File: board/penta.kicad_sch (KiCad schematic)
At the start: 184 parts, among them J1 USB_C_Receptacle, J2 USB_C_Receptacle, J3 Conn_01x03_Pin, Q1 Q_NMOS_SGD, SW1 SW_Push, U1 3.3V LDO, U2 RP2040, U3 QSPI Flash, U4 MSUSB30, U5 USBLC6-2P6, Y1 12MHz

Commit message: kicad format update
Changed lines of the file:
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@@
 (kicad_sch
-	(version 20231120)
+	(version 20250114)
 	(generator "eeschema")
-	(generator_version "8.0")
+	(generator_version "9.0")
 	(paper "A4")
+	(text "layout close to rp2040"
+		(exclude_from_sim no)
+		(at 121.92 44.45 0)
+		(effects
+			(font
+				(size 1.27 1.27)
+			)
+			(justify left bottom)
+		)
+	)
+	(text "LRCLK gpio must be CLK+1"
+		(exclude_from_sim no)
+		(at 214.122 94.742 0)
+		(effects
+			(font
+				(size 1.27 1.27)
+			)
+			(justify left)
+		)
+	)
+	(text "Pixels Load Switch"
+		(exclude_from_sim no)
+		(at 261.366 78.486 0)
+		(effects
+			(font
+				(size 1.5 1.5)
+			)
+		)
+	)
+	(text "pio requirement:\ntouch pins must be contiguous gpios"
+		(exclude_from_sim no)
+		(at 231.394 50.038 0)
+		(effects
+			(font
+				(size 1.27 1.27)
+			)
+			(justify left)
+		)
+	)
 	(junction
 		(at 397.51 234.95)
@@
 		)
 	)
-	(text "layout close to rp2040"
-		(exclude_from_sim no)
-		(at 121.92 44.45 0)
-		(effects
-			(font
-				(size 1.27 1.27)
-			)
-			(justify left bottom)
-		)
-	)
-	(text "LRCLK gpio must be CLK+1"
-		(exclude_from_sim no)
-		(at 214.122 94.742 0)
-		(effects
-			(font
-				(size 1.27 1.27)
-			)
-			(justify left)
-		)
-	)
-	(text "Pixels Load Switch"
-		(exclude_from_sim no)
-		(at 261.366 78.486 0)
-		(effects
-			(font
-				(size 1.5 1.5)
-			)
-		)
-	)
-	(text "pio requirement:\ntouch pins must be contiguous gpios"
-		(exclude_from_sim no)
-		(at 231.394 50.038 0)
-		(effects
-			(font
-				(size 1.27 1.27)
-			)
-			(justify left)
-		)
-	)
 	(label "UART0_TX"
 		(at 201.93 85.09 0)
-		(fields_autoplaced yes)
 		(effects
 			(font
@@
 	(label "LED_DATA"
 		(at 328.93 26.67 180)
-		(fields_autoplaced yes)
 		(effects
 			(font
@@
 	(label "EN_PIXELS"
 		(at 201.93 100.33 0)
-		(fields_autoplaced yes)
 		(effects
 			(font
@@
 	(label "PDM_LRCLK"
 		(at 261.62 138.43 0)
-		(fields_autoplaced yes)
 		(effects
 			(font
@@
 	(label "USB_D+"
 		(at 69.85 96.52 180)
-		(fields_autoplaced yes)
 		(effects
 			(font
@@
 	(label "~{USB_BOOT}"
 		(at 123.19 62.23 0)
-		(fields_autoplaced yes)
 		(effects
 			(font
@@
 	(label "SWCLK"
 		(at 143.51 110.49 0)
-		(fields_autoplaced yes)
 		(effects
 			(font
@@
 	(label "USB_D-_PORT"
 		(at 57.15 59.69 270)
-		(fields_autoplaced yes)
 		(effects
 			(font
@@
 	(label "USB_D-_IN"
 		(at 44.45 38.1 0)
-		(fields_autoplaced yes)
 		(effects
 			(font
@@
 	(label "USB_D+"
 		(at 125.73 48.26 0)
-		(fields_autoplaced yes)
 		(effects
 			(font
@@
 	(label "PXL_GND"
 		(at 264.16 87.63 0)
-		(fields_autoplaced yes)
 		(effects
 			(font
@@
 	(label "USB2_D+"
 		(at 45.72 140.97 0)
-		(fields_autoplaced yes)
 		(effects
 			(font
@@
 	(label "QSPI_SCK"
 		(at 167.64 157.48 0)
-		(fields_autoplaced yes)
 		(effects
 			(font
@@
 	(label "QSPI3"
 		(at 142.24 74.93 0)
-		(fields_autoplaced yes)
 		(effects
 			(font
@@
 	(label "USB2_D-"
 		(at 45.72 138.43 0)
-		(fields_autoplaced yes)
 		(effects
 			(font
@@
 	(label "PXL_GND"
 		(at 331.47 274.32 180)
-		(fields_autoplaced yes)
 		(effects
 			(font
@@
 	(label "PXL_GND"
 		(at 331.47 34.29 180)
-		(fields_autoplaced yes)
 		(effects
 			(font
@@
 	(label "UART0_RX"
 		(at 201.93 87.63 0)
-		(fields_autoplaced yes)
 		(effects
 			(font
@@
 	(label "PDM_DATA"
 		(at 261.62 140.97 0)
-		(fields_autoplaced yes)
 		(effects
 			(font
@@
 	(label "USB_D+_IN"
 		(at 44.45 40.64 0)
-		(fields_autoplaced yes)
 		(effects
 			(font
@@
 	(label "QSPI1"
 		(at 129.54 153.67 180)
-		(fields_autoplaced yes)
 		(effects
 			(font
@@
 	(label "USB2_D-"
 		(at 222.25 85.09 0)
-		(fields_autoplaced yes)
 		(effects
 			(font
@@
 	(label "EN_PIXELS"
 		(at 252.73 100.33 90)
-		(fields_autoplaced yes)
 		(effects
 			(font
@@
 	(label "QSPI0"
 		(at 142.24 67.31 0)
-		(fields_autoplaced yes)
 		(effects
 			(font
@@
 	(label "USB_D-"
 		(at 92.71 99.06 0)
-		(fields_autoplaced yes)
 		(effects
 			(font
@@
 	(label "USB_D+_PORT"
 		(at 69.85 101.6 180)
-		(fields_autoplaced yes)
 		(effects
 			(font
@@
 	(label "PXL_GND"
 		(at 331.47 114.3 180)
-		(fields_autoplaced yes)
 		(effects
 			(font
@@
 	(label "PXL_GND"
 		(at 331.47 154.94 180)
-		(fields_autoplaced yes)
 		(effects
 			(font
@@
 	(label "UART1_RX"
 		(at 92.71 101.6 0)
-		(fields_autoplaced yes)
 		(effects
 			(font
@@
 	(label "QSPI_SS"
 		(at 142.24 62.23 0)
-		(fields_autoplaced yes)
 		(effects
 			(font
@@
 	(label "PXL_GND"
 		(at 331.47 74.93 180)
-		(fields_autoplaced yes)
 		(effects
 			(font
@@
 	(label "LED_DATA"
 		(at 201.93 59.69 0)
-		(fields_autoplaced yes)
 		(effects
 			(font
@@
 	(label "USB_D+_PORT"
 		(at 54.61 59.69 270)
-		(fields_autoplaced yes)
 		(effects
 			(font
@@
 	(label "PXL_GND"
 		(at 331.47 194.31 180)
-		(fields_autoplaced yes)
 		(effects
 			(font
@@
 	(label "PDM_CLK"
 		(at 261.62 143.51 0)
-		(fields_autoplaced yes)
 		(effects
 			(font
@@
 	(label "USB_D-"
 		(at 125.73 54.61 0)
-		(fields_autoplaced yes)
 		(effects
 			(font
@@
 	(label "PDM_DATA"
 		(at 201.93 95.25 0)
-		(fields_autoplaced yes)
 		(effects
 			(font
@@
 	(label "USB2_D+"
 		(at 222.25 87.63 0)
-		(fields_autoplaced yes)
 		(effects
 			(font
@@
 	(label "USBMUX_SELECT"
 		(at 201.93 102.87 0)
-		(fields_autoplaced yes)
 		(effects
 			(font
@@
 	(label "UART1_RX"
 		(at 201.93 107.95 0)
-		(fields_autoplaced yes)
 		(effects
 			(font
@@
 	(label "PXL_GND"
 		(at 331.47 234.95 180)
-		(fields_autoplaced yes)
 		(effects
 			(font
@@
 	(label "QSPI0"
 		(at 167.64 160.02 0)
-		(fields_autoplaced yes)
 		(effects
 			(font
@@
 	(label "QSPI3"
 		(at 167.64 154.94 0)
-		(fields_autoplaced yes)
 		(effects
 			(font
@@
 	(label "QSPI1"
 		(at 142.24 69.85 0)
-		(fields_autoplaced yes)
 		(effects
 			(font
@@
 	(label "UART1_TX"
 		(at 201.93 105.41 0)
-		(fields_autoplaced yes)
 		(effects
 			(font
@@
 	(label "QSPI_SS"
 		(at 129.54 151.13 180)
-		(fields_autoplaced yes)
 		(effects
 			(font
@@
 	(label "USBMUX_SELECT"
 		(at 69.85 93.98 180)
-		(fields_autoplaced yes)
 		(effects
 			(font
@@
 	(label "PDM_CLK"
 		(at 201.93 90.17 0)
-		(fields_autoplaced yes)
 		(effects
 			(font
@@
 	(label "PDM_LRCLK"
 		(at 201.93 92.71 0)
-		(fields_autoplaced yes)
 		(effects
 			(font
@@
 	(label "QSPI2"
 		(at 142.24 72.39 0)
-		(fields_autoplaced yes)
 		(effects
 			(font
@@
 	(label "SWD"
 		(at 143.51 113.03 0)
-		(fields_autoplaced yes)
 		(effects
 			(font
@@
 	(label "QSPI_SCK"
 		(at 139.7 77.47 0)
-		(fields_autoplaced yes)
 		(effects
 			(font
@@
 	(label "UART1_TX"
 		(at 69.85 99.06 180)
-		(fields_autoplaced yes)
 		(effects
 			(font
@@
 	(label "QSPI2"
 		(at 129.54 156.21 180)
-		(fields_autoplaced yes)
 		(effects
 			(font
@@
 	(label "USB_D-_PORT"
 		(at 92.71 104.14 0)
-		(fields_autoplaced yes)
 		(effects
 			(font
@@
 		)
 	)
+	(embedded_fonts no)
 )

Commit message: mosfet GSD was actually correct so change it back. the dim pixel issue was current leaking through data line, already fixed in software in main
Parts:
- removed Q1: Q_NMOS_SGD, Package_TO_SOT_SMD:SOT-23, symbol Device:Q_NMOS_SGD
- added Q1: Q_NMOS_GSD, symbol Transistor_FET:Q_NMOS_GSD
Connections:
- net EN_PIXELS: now also Q1.1 (G)
- net GND: now also Q1.2 (S)
- net PXL_GND: now also Q1.3 (D)
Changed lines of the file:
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@@
 	)
 	(junction
-		(at 473.71 219.71)
-		(diameter 0)
-		(color 0 0 0 0)
-	)
-	(junction
 		(at 443.23 170.18)
 		(diameter 0)
@@
 	)
 	(junction
-		(at 473.71 59.69)
-		(diameter 0)
-		(color 0 0 0 0)
-	)
-	(junction
 		(at 458.47 74.93)
 		(diameter 0)
@@
 	)
 	(junction
-		(at 473.71 139.7)
-		(diameter 0)
-		(color 0 0 0 0)
-	)
-	(junction
 		(at 336.55 99.06)
 		(diameter 0)
@@
 	(wire
 		(pts
-			(xy 473.71 58.42) (xy 473.71 59.69)
-		)
-		(stroke
-			(width 0)
-			(type default)
-		)
-	)
-	(wire
-		(pts
 			(xy 336.55 139.7) (xy 351.79 139.7)
 		)
@@
 	(wire
 		(pts
-			(xy 473.71 138.43) (xy 473.71 139.7)
-		)
-		(stroke
-			(width 0)
-			(type default)
-		)
-	)
-	(wire
-		(pts
 			(xy 209.55 22.86) (xy 219.71 22.86)
 		)
@@
 	(wire
 		(pts
-			(xy 473.71 218.44) (xy 473.71 219.71)
-		)
-		(stroke
-			(width 0)
-			(type default)
-		)
-	)
-	(wire
-		(pts
 			(xy 50.8 30.48) (xy 50.8 27.94)
 		)
@@
 	)
 	(symbol
-		(lib_id "Device:Q_NMOS_SGD")
-		(at 261.62 100.33 0)
+		(lib_id "power:GND")
+		(at 264.16 107.95 0)
 		(unit 1)
 		(exclude_from_sim no)
@@
 		(on_board yes)
 		(dnp no)
-		(fields_autoplaced yes)
-		(property "Reference" "Q1"
-			(at 266.827 99.1178 0)
-			(effects
-				(font
-					(size 1.27 1.27)
-				)
-				(justify left)
-			)
-		)
-		(property "Value" "Q_NMOS_SGD"
-			(at 266.827 101.5421 0)
-			(effects
-				(font
-					(size 1.27 1.27)
-				)
-				(justify left)
-			)
-		)
-		(property "Footprint" "Package_TO_SOT_SMD:SOT-23"
-			(at 266.7 97.79 0)
+		(property "Reference" "#PWR03"
+			(at 264.16 114.3 0)
 			(effects
 				(font
@@
 			)
 		)
-		(property "Datasheet" "~"
-			(at 261.62 100.33 0)
+		(property "Value" "GND"
+			(at 264.16 112.522 90)
 			(effects
 				(font
 					(size 1.27 1.27)
 				)
-				(hide yes)
 			)
 		)
-		(property "Description" "N-MOSFET transistor, source/gate/drain"
-			(at 261.62 100.33 0)
+		(property "Footprint" ""
+			(at 264.16 107.95 0)
 			(effects
 				(font
@@
 			)
 		)
-		(property "Designation" "SI2302"
-			(at 261.62 100.33 0)
+		(property "Datasheet" ""
+			(at 264.16 107.95 0)
 			(effects
 				(font
@@
 			)
 		)
-		(property "LCSC" "C727152"
-			(at 261.62 100.33 0)
+		(property "Description" "Power symbol creates a global label with name \"GND\" , ground"
+			(at 264.16 107.95 0)
 			(effects
 				(font
@@
 			)
 		)
-		(pin "2"
-		)
-		(pin "3"
-		)
 		(pin "1"
 		)
@@
 			(project "penta"
 				(path "/2e8b15b9-33da-4001-b66c-591b57065bcb"
-					(reference "Q1")
+					(reference "#PWR03")
 					(unit 1)
 				)
@@
 	(symbol
 		(lib_id "power:GND")
-		(at 264.16 107.95 0)
+		(at 209.55 35.56 0)
 		(unit 1)
 		(exclude_from_sim no)
@@
 		(on_board yes)
 		(dnp no)
-		(property "Reference" "#PWR03"
-			(at 264.16 114.3 0)
+		(fields_autoplaced yes)
+		(property "Reference" "#PWR021"
+			(at 209.55 41.91 0)
 			(effects
 				(font
@@
 		)
 		(property "Value" "GND"
-			(at 264.16 112.522 90)
+			(at 209.55 39.6931 0)
 			(effects
 				(font
@@
 		)
 		(property "Footprint" ""
-			(at 264.16 107.95 0)
+			(at 209.55 35.56 0)
 			(effects
 				(font
@@
 		)
 		(property "Datasheet" ""
-			(at 264.16 107.95 0)
+			(at 209.55 35.56 0)
 			(effects
 				(font
@@
 			)
 		)
-		(property "Description" "Power symbol creates a global label with name \"GND\" , ground"
-			(at 264.16 107.95 0)
+		(property "Description" ""
+			(at 209.55 35.56 0)
 			(effects
 				(font
@@
 			(project "penta"
 				(path "/2e8b15b9-33da-4001-b66c-591b57065bcb"
-					(reference "#PWR03")
+					(reference "#PWR021")
 					(unit 1)
 				)
@@
 	)
 	(symbol
-		(lib_id "power:GND")
-		(at 209.55 35.56 0)
+		(lib_id "Transistor_FET:Q_NMOS_GSD")
+		(at 261.62 100.33 0)
 		(unit 1)
 		(exclude_from_sim no)
@@
 		(dnp no)
 		(fields_autoplaced yes)
-		(property "Reference" "#PWR021"
-			(at 209.55 41.91 0)
+		(property "Reference" "Q1"
+			(at 266.827 99.1178 0)
 			(effects
 				(font
 					(size 1.27 1.27)
 				)
-				(hide yes)
+				(justify left)
 			)
 		)
-		(property "Value" "GND"
-			(at 209.55 39.6931 0)
+		(property "Value" "Q_NMOS_GSD"
+			(at 266.827 101.5421 0)
 			(effects
 				(font
 					(size 1.27 1.27)
 				)
+				(justify left)
 			)
 		)
 		(property "Footprint" ""
-			(at 209.55 35.56 0)
+			(at 266.7 97.79 0)
 			(effects
 				(font
@@
 			)
 		)
-		(property "Datasheet" ""
-			(at 209.55 35.56 0)
+		(property "Datasheet" "~"
+			(at 261.62 100.33 0)
 			(effects
 				(font
@@
 			)
 		)
-		(property "Description" ""
-			(at 209.55 35.56 0)
+		(property "Description" "N-MOSFET transistor, gate/source/drain"
+			(at 261.62 100.33 0)
 			(effects
 				(font
@@
 			)
 		)
+		(property "Designation" ""
+			(at 261.62 100.33 0)
+			(effects
+				(font
+					(size 1.27 1.27)
+				)
+				(hide yes)
+			)
+		)
+		(pin "2"
+		)
 		(pin "1"
 		)
+		(pin "3"
+		)
 		(instances
-			(project "penta"
+			(project ""
 				(path "/2e8b15b9-33da-4001-b66c-591b57065bcb"
-					(reference "#PWR021")
+					(reference "Q1")
 					(unit 1)
 				)
@@
 			)
 		)
-		(property "Description" ""
+		(property "Description" "Resistor, small symbol"
 			(at 137.16 54.61 0)
 			(effects
@@
 			)
 		)
-		(property "Description" ""
+		(property "Description" "Resistor, small symbol"
 			(at 219.71 87.63 0)
 			(effects
@@
 			)
 		)
-		(property "Description" ""
+		(property "Description" "Resistor, small symbol"
 			(at 129.54 144.78 0)
 			(effects
@@
 			)
 		)
-		(property "Description" ""
+		(property "Description" "Resistor, small symbol"
 			(at 137.16 48.26 0)
 			(effects
@@
 			)
 		)
-		(property "Description" ""
+		(property "Description" "Four pin crystal, GND on pins 2 and 4, small symbol"
 			(at 135.89 95.25 0)
 			(effects
@@
 			)
 		)
-		(property "Description" ""
+		(property "Description" "Resistor, small symbol"
 			(at 110.49 101.6 0)
 			(effects
@@
 			)
 		)
-		(property "Description" ""
+		(property "Description" "Resistor, small symbol"
 			(at 219.71 85.09 0)
 			(effects

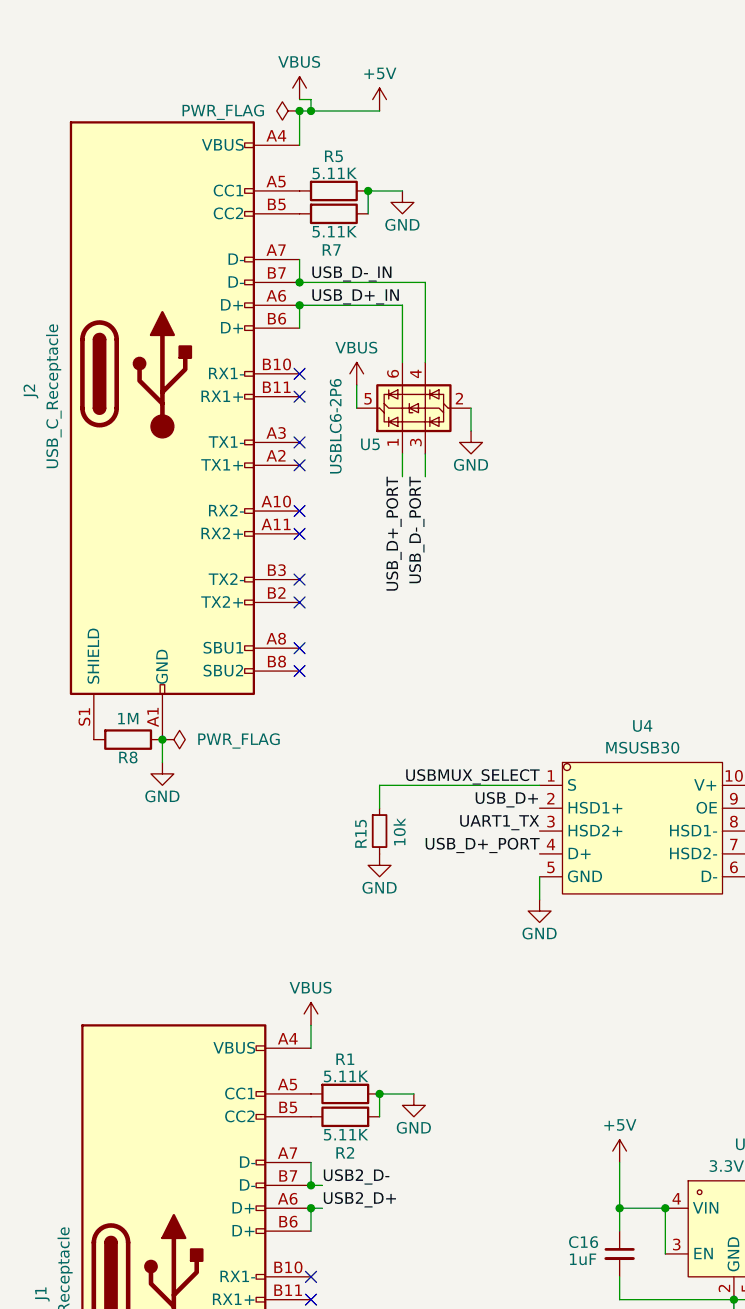
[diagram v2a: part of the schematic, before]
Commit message: many passives -> Basic JLC parts; fix mirrored silkscreen labels; fix Q1 missing a footprint in sch
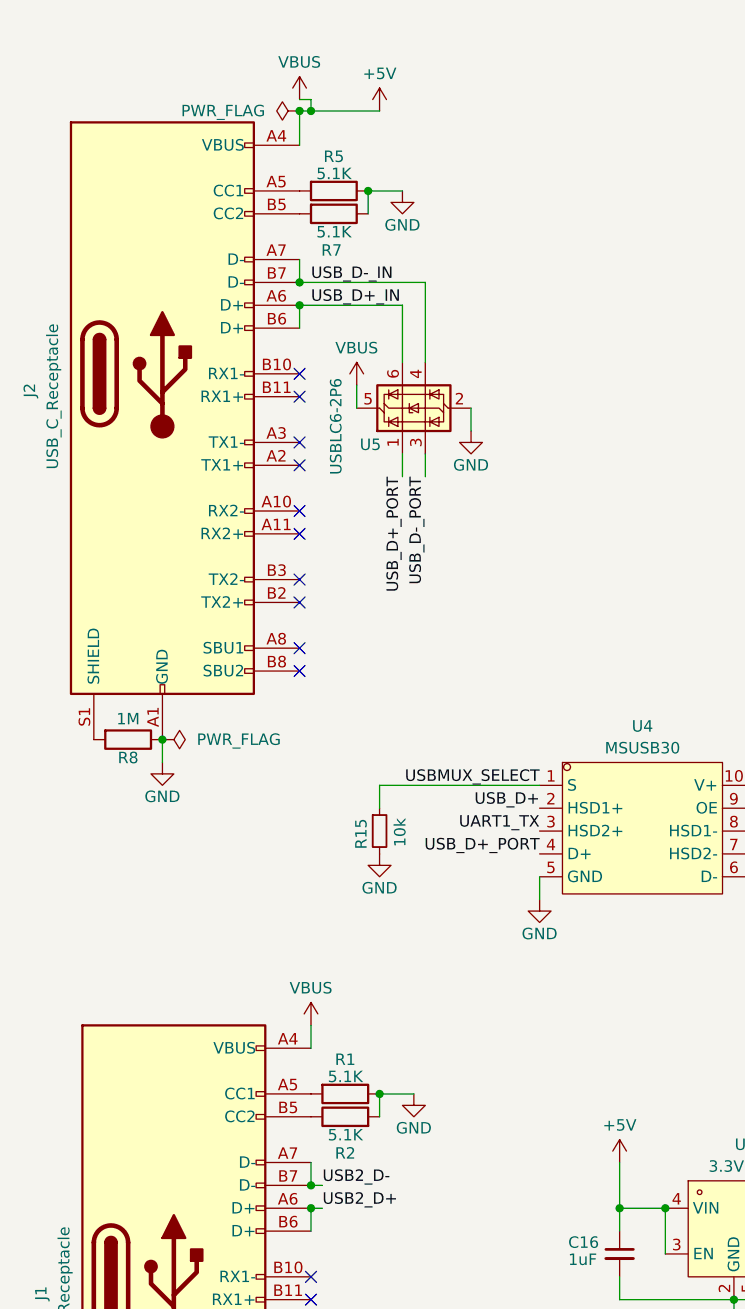
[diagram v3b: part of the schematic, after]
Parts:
- C1, C10, C11, C17, C19, C2, C25, C3, C4, C5, C6, C7, C8, C9: Designation CC0402KRX7R7BB104 -> CL05B104KO5NNNC; LCSC C60474 -> C1525
- C12, C13, C16, C18: Designation CL05A105KP5NNNC -> CL05A105KA5NQNC; LCSC C14445 -> C52923
- C14, C15: Designation CC0402FRNPO9BN120 -> 0402CG120J500NT; LCSC C326662 -> C1547
- C20, C21, C22, C23, C24: Designation (none) -> CL05A106MQ5NUNC; LCSC (none) -> C15525
- Q1: footprint (none) -> Package_TO_SOT_SMD:SOT-23
- R1, R2, R5, R7: value 5.11K -> 5.1K; Designation RC0402FR-075K11L -> 0402WGF5101TCE; LCSC C274895 -> C25905
- R10, R9: Designation RC0402FR-071KL -> 0402WGF1001TCE; LCSC C106235 -> C11702
- R11, R8: Designation RC0402JR-071ML -> 0402WGF1004TCE; LCSC C93949 -> C26083
- R12, R15: Designation RC0402FR-0710KL -> 0402WGF1002TCE; LCSC C60490 -> C25744
